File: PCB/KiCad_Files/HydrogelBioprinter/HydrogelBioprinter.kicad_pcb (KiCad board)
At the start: 2 copper layers, 22 parts, among them Q1 RFP30N06LE, U1 STM32F407VGT6, U3 MAX6675ISA_, U4 MAX6675ISA_, U5 MAX6675ISA_, U6 MAX6675ISA_, U7 HX711

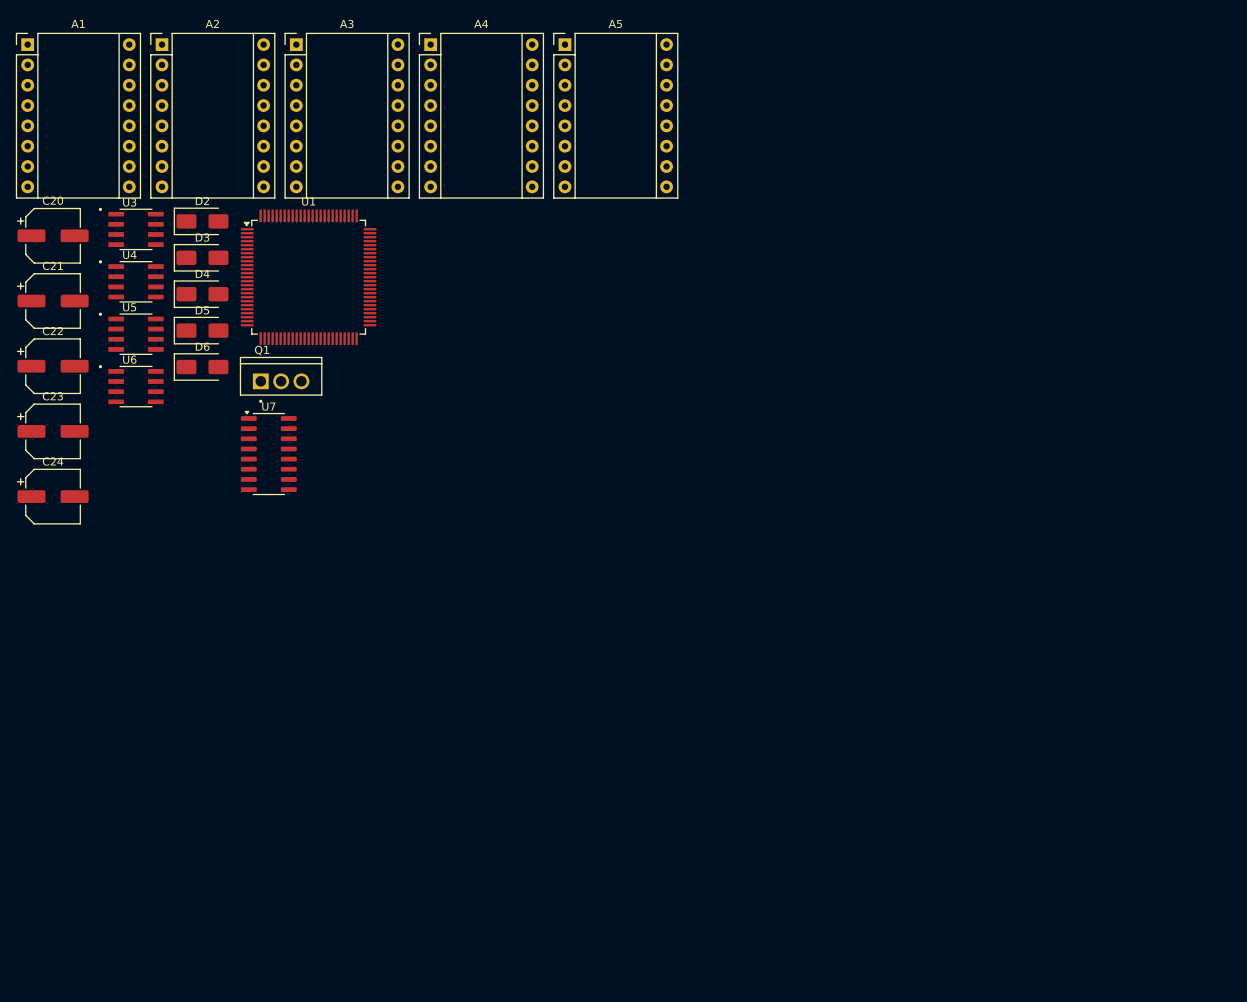
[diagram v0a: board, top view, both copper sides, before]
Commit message: Finished Drivers and Thermocouple Amplifier connections in KiCad Schematic
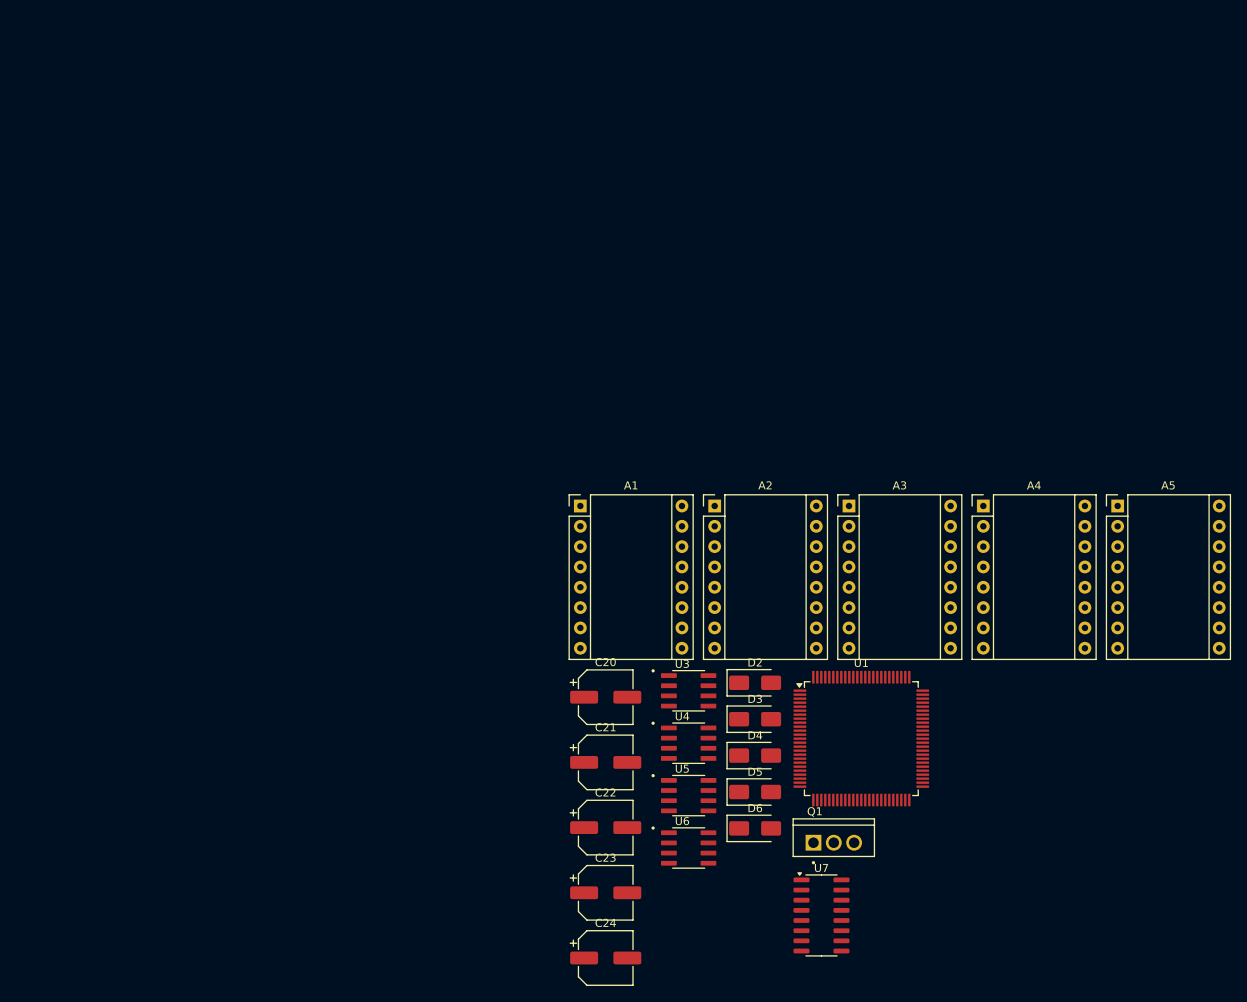
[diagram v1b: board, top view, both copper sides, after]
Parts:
- moved A1 90.0 mm to (70.6, 59.2)
- moved A2 90.0 mm to (87.4, 59.2)
- moved A3 90.0 mm to (104.2, 59.2)
- moved A4 90.0 mm to (121.0, 59.2)
- moved A5 90.0 mm to (137.8, 59.2)
- moved C20 90.0 mm to (73.8, 83.1)
- moved C21 90.0 mm to (73.8, 91.3)
- moved C22 90.0 mm to (73.8, 99.4)
- moved C23 90.0 mm to (73.8, 107.6)
- moved C24 90.0 mm to (73.8, 115.7)
- moved D2 90.0 mm to (92.5, 81.3)
- moved D3 90.0 mm to (92.5, 85.9)
- moved D4 90.0 mm to (92.5, 90.4)
- moved D5 90.0 mm to (92.5, 95.0)
- moved D6 90.0 mm to (92.5, 99.5)
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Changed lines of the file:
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@@
 	(footprint "MAX6675ISA_:SOIC127P600X175-8N"
 		(layer "F.Cu")
-		(at 15.095 44.295)
+		(at 84.18 101.97)
 		(property "Reference" "U6"
 			(at -0.795 -3.332 0)
@@
 	(footprint "Diode_SMD:D_SMA"
 		(layer "F.Cu")
-		(at 23.4 37.295)
+		(at 92.485 94.97)
 		(descr "Diode SMA (DO-214AC)")
 		(tags "Diode SMA (DO-214AC)")
@@
 	(footprint "Diode_SMD:D_SMA"
 		(layer "F.Cu")
-		(at 23.4 32.745)
+		(at 92.485 90.42)
 		(descr "Diode SMA (DO-214AC)")
 		(tags "Diode SMA (DO-214AC)")
@@
 	(footprint "MAX6675ISA_:SOIC127P600X175-8N"
 		(layer "F.Cu")
-		(at 15.095 37.745)
+		(at 84.18 95.42)
 		(property "Reference" "U5"
 			(at -0.795 -3.332 0)
@@
 	(footprint "MAX6675ISA_:SOIC127P600X175-8N"
 		(layer "F.Cu")
-		(at 15.095 24.645)
+		(at 84.18 82.32)
 		(property "Reference" "U3"
 			(at -0.795 -3.332 0)
@@
 	(footprint "Package_QFP:LQFP-100_14x14mm_P0.5mm"
 		(layer "F.Cu")
-		(at 36.675 30.625)
+		(at 105.76 88.3)
 		(descr "LQFP, 100 Pin (https://www.nxp.com/docs/en/package-information/SOT407-1.pdf), generated with kicad-footprint-generator ipc_gullwing_generator.py")
 		(tags "LQFP QFP")
@@
 	(footprint "RFP30N06LE:TRANS_RFP30N06LE"
 		(layer "F.Cu")
-		(at 33.235 43.635)
+		(at 102.32 101.31)
 		(property "Reference" "Q1"
 			(at -2.368715 -3.891095 0)
@@
 	(footprint "Diode_SMD:D_SMA"
 		(layer "F.Cu")
-		(at 23.4 41.845)
+		(at 92.485 99.52)
 		(descr "Diode SMA (DO-214AC)")
 		(tags "Diode SMA (DO-214AC)")
@@
 	(footprint "Capacitor_SMD:CP_Elec_6.3x7.7"
 		(layer "F.Cu")
-		(at 4.725 25.445)
+		(at 73.81 83.12)
 		(descr "SMD capacitor, aluminum electrolytic, Nichicon, 6.3x7.7mm")
 		(tags "capacitor electrolytic")
@@
 	(footprint "Module:Pololu_Breakout-16_15.2x20.3mm"
 		(layer "F.Cu")
-		(at 68.715 1.545)
+		(at 137.8 59.22)
 		(descr "Pololu Breakout 16-pin 15.2x20.3mm 0.6x0.8\\")
 		(tags "Pololu Breakout")
@@
 	(footprint "Module:Pololu_Breakout-16_15.2x20.3mm"
 		(layer "F.Cu")
-		(at 1.555 1.545)
+		(at 70.64 59.22)
 		(descr "Pololu Breakout 16-pin 15.2x20.3mm 0.6x0.8\\")
 		(tags "Pololu Breakout")
@@
 	(footprint "Module:Pololu_Breakout-16_15.2x20.3mm"
 		(layer "F.Cu")
-		(at 35.135 1.545)
+		(at 104.22 59.22)
 		(descr "Pololu Breakout 16-pin 15.2x20.3mm 0.6x0.8\\")
 		(tags "Pololu Breakout")
@@
 	(footprint "Capacitor_SMD:CP_Elec_6.3x7.7"
 		(layer "F.Cu")
-		(at 4.725 49.895)
+		(at 73.81 107.57)
 		(descr "SMD capacitor, aluminum electrolytic, Nichicon, 6.3x7.7mm")
 		(tags "capacitor electrolytic")
@@
 	(footprint "Capacitor_SMD:CP_Elec_6.3x7.7"
 		(layer "F.Cu")
-		(at 4.725 33.595)
+		(at 73.81 91.27)
 		(descr "SMD capacitor, aluminum electrolytic, Nichicon, 6.3x7.7mm")
 		(tags "capacitor electrolytic")
@@
 	(footprint "Package_SO:SOP-16_3.9x9.9mm_P1.27mm"
 		(layer "F.Cu")
-		(at 31.695 52.725)
+		(at 100.78 110.4)
 		(descr "SOP, 16 Pin (https://www.diodes.com/assets/Datasheets/PAM8403.pdf), generated with kicad-footprint-generator ipc_gullwing_generator.py")
 		(tags "SOP SO")
@@
 	(footprint "Capacitor_SMD:CP_Elec_6.3x7.7"
 		(layer "F.Cu")
-		(at 4.725 41.745)
+		(at 73.81 99.42)
 		(descr "SMD capacitor, aluminum electrolytic, Nichicon, 6.3x7.7mm")
 		(tags "capacitor electrolytic")
@@
 	(footprint "Module:Pololu_Breakout-16_15.2x20.3mm"
 		(layer "F.Cu")
-		(at 18.345 1.545)
+		(at 87.43 59.22)
 		(descr "Pololu Breakout 16-pin 15.2x20.3mm 0.6x0.8\\")
 		(tags "Pololu Breakout")
@@
 	(footprint "Capacitor_SMD:CP_Elec_6.3x7.7"
 		(layer "F.Cu")
-		(at 4.725 58.045)
+		(at 73.81 115.72)
 		(descr "SMD capacitor, aluminum electrolytic, Nichicon, 6.3x7.7mm")
 		(tags "capacitor electrolytic")
@@
 	(footprint "Diode_SMD:D_SMA"
 		(layer "F.Cu")
-		(at 23.4 28.195)
+		(at 92.485 85.87)
 		(descr "Diode SMA (DO-214AC)")
 		(tags "Diode SMA (DO-214AC)")
@@
 	(footprint "MAX6675ISA_:SOIC127P600X175-8N"
 		(layer "F.Cu")
-		(at 15.095 31.195)
+		(at 84.18 88.87)
 		(property "Reference" "U4"
 			(at -0.795 -3.332 0)
@@
 	(footprint "Diode_SMD:D_SMA"
 		(layer "F.Cu")
-		(at 23.4 23.645)
+		(at 92.485 81.32)
 		(descr "Diode SMA (DO-214AC)")
 		(tags "Diode SMA (DO-214AC)")
@@
 	(footprint "Module:Pololu_Breakout-16_15.2x20.3mm"
 		(layer "F.Cu")
-		(at 51.925 1.545)
+		(at 121.01 59.22)
 		(descr "Pololu Breakout 16-pin 15.2x20.3mm 0.6x0.8\\")
 		(tags "Pololu Breakout")
